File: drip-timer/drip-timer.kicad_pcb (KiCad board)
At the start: 2 copper layers, 43.1 x 56.7 mm, 9 parts, among them J1 BATT, J2 VALVE, J3 FLASH, K1 DIPxx-1Axx-11x, SW1 GO, U1 ProMicro, U3 MOC3021

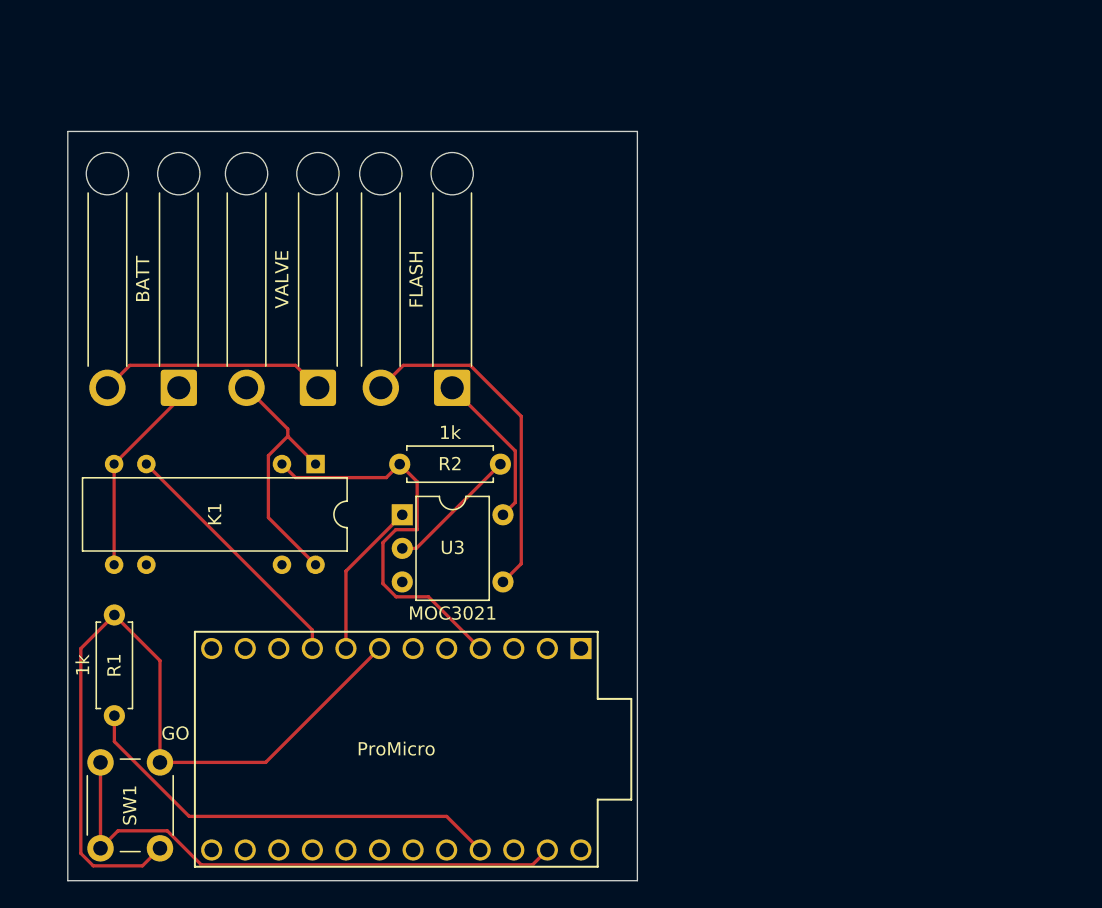
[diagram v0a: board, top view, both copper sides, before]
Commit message: Add files via upload
Many updates, including switches and pots for better control, layout changes etc
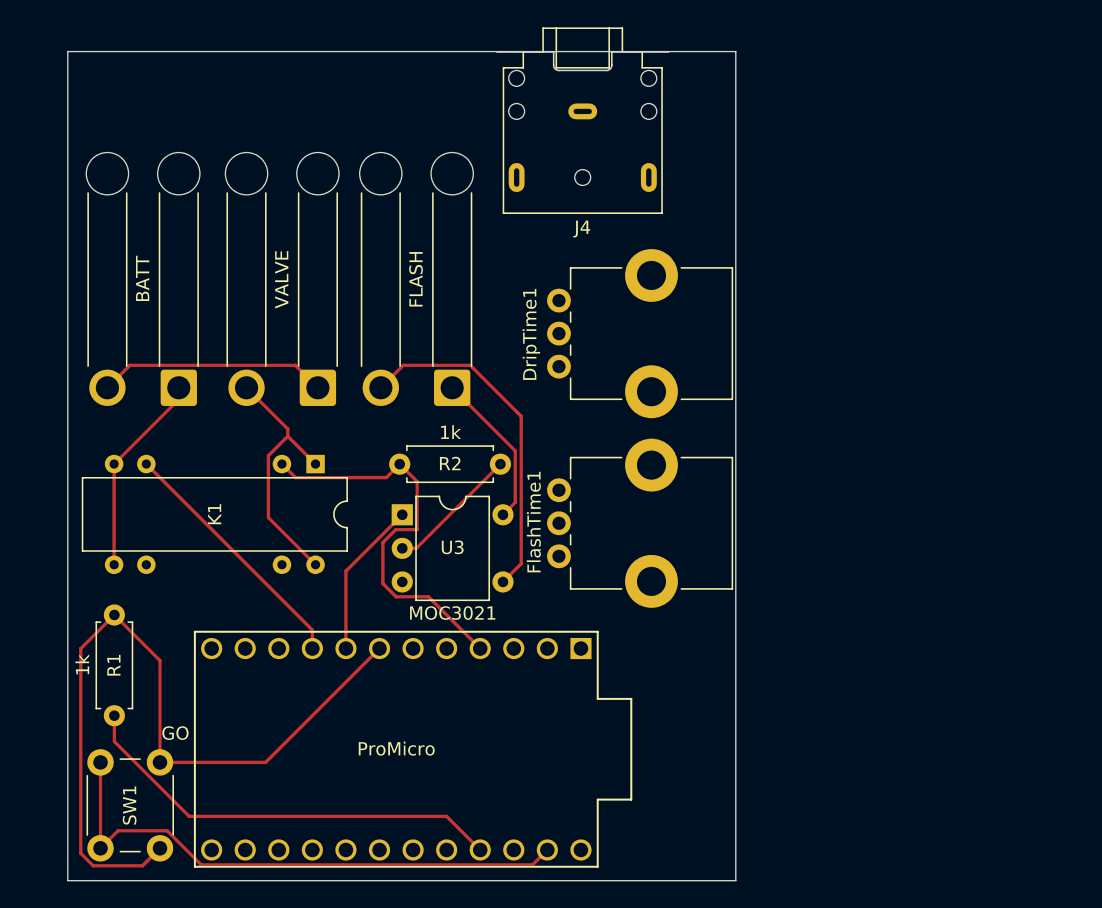
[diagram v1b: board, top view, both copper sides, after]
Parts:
- added DripTime1: R_Potentiometer, Potentiometer_THT:Potentiometer_Bourns_PTV09A-1_Single_Vertical, F.Cu at (165.7, 62.5)
- added FlashTime1: R_Potentiometer, Potentiometer_THT:Potentiometer_Bourns_PTV09A-1_Single_Vertical, F.Cu at (165.7, 76.8)
- added J4: Flash TS, Connector_Audio:Jack_3.5mm_CUI_SJ1-3523N_Horizontal, F.Cu at (167.5, 43.2)
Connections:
- net Net-(U1-VCC) renamed VCC
- K1 pad 2: Net-(K1-Pad2) -> GND
- R2 pad 2: Net-(K1-Pad2) -> GND
- SW1 pad 1: Net-(SW1-Pad1) -> GND
- U1 pad 18: unconnected-(U1-F6-Pad18) -> Net-(U1-F6)
- U1 pad 19: unconnected-(U1-F5-Pad19) -> Net-(U1-F5)
- U1 pad 2: unconnected-(U1-RX-Pad2) -> Net-(SW2-B)
- U1 pad 23: Net-(SW1-Pad1) -> GND
- U1 pad 3: unconnected-(U1-GND-Pad3) -> GND
- U1 pad 4: Net-(K1-Pad2) -> GND
- U3 pad 4: Net-(J3-Pin_2) -> Net-(J3-Pin_1)
- U3 pad 6: Net-(J3-Pin_1) -> Net-(J3-Pin_2)
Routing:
- net GND: track 0.00 -> 73.1 mm
- net Net-(SW1-Pad1): track 42.4 -> 0.00 mm
- net Net-(K1-Pad2): track 30.8 -> 0.00 mm
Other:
- board size 43.1 x 56.7 mm -> 50.5 x 62.7 mm

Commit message: completed work on v0.1 of pcb
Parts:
- added REF**: MountingHole_3.2mm_M3_DIN965_Pad, MountingHole:MountingHole_3.2mm_M3_DIN965_Pad, F.Cu at (129.0, 84.3)
- added REF**: MountingHole_3.2mm_M3_DIN965_Pad, MountingHole:MountingHole_3.2mm_M3_DIN965_Pad, F.Cu at (201.2, 42.2)
- added REF**: MountingHole_3.2mm_M3_DIN965_Pad, MountingHole:MountingHole_3.2mm_M3_DIN965_Pad, F.Cu at (129.0, 42.2)
- added REF**: MountingHole_3.2mm_M3_DIN965_Pad, MountingHole:MountingHole_3.2mm_M3_DIN965_Pad, F.Cu at (201.2, 84.3)
- added SW2: Drips, Button_Switch_THT:SW_E-Switch_EG1271_SPDT, F.Cu at (187.1, 78.7)
- DripTime1, FlashTime1: value R_Potentiometer -> 10k
- J4: value Flash TS -> Flash Trigger
- U3: value MOC3021 -> MOC3021S; footprint Package_DIP:Toshiba_11-7A9 -> Package_DIP:SMDIP-6_W7.62mm
- moved U1 49.8 mm to (189.0, 56.6), turned to -90 degrees
- moved R1 26.6 mm to (154.7, 67.3), turned to 0 degrees
- moved SW1 21.4 mm to (141.9, 80.5), turned to 180 degrees
- moved U3 20.9 mm to (172.2, 63.8), turned to 90 degrees
- moved DripTime1 18.0 mm to (151.6, 73.7), turned to -90 degrees
- moved J3 8.99 mm to (163.7, 57.5)
- moved K1 8.39 mm to (147.3, 61.5)
- moved J2 8.03 mm to (152.1, 57.5)
- moved J1 7.43 mm to (140.4, 57.5)
- moved R2 6.70 mm to (162.3, 63.2)
- moved J4 5.60 mm to (173.1, 43.1)
- moved FlashTime1 4.69 mm to (169.2, 73.7), turned to -90 degrees
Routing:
- net GND: track 73.1 -> 165.0 mm
- net VCC: track 33.0 -> 87.7 mm
- net Net-(SW2-B): track 0.00 -> 53.7 mm
- net Net-(U1-D7): track 19.2 -> 72.7 mm
- net Net-(U1-F5): track 0.00 -> 50.1 mm
- net Net-(U1-F6): track 0.00 -> 31.4 mm
- net Net-(J3-Pin_1): track 12.0 -> 30.6 mm
- net Net-(J2-Pin_2): track 19.7 -> 11.9 mm
- net Net-(U1-D4): track 58.8 -> 53.4 mm
- net Net-(U1-C6): track 11.9 -> 14.6 mm
- net Net-(R2-Pad1): track 10.1 -> 12.8 mm
- net Net-(J1-Pin_1): track 15.4 -> 17.6 mm
- net Net-(J1-Pin_2): track 17.3 -> 18.5 mm
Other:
- board size 50.5 x 62.7 mm -> 79.2 x 49 mm
- board text added: "1"
- board text added: "2"
- board text added: "v0.1 for Trev"
